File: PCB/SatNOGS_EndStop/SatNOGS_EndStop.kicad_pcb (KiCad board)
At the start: 2 copper layers, 47 x 14 mm, 7 parts, among them P1 CONN_01X03, U1 TCST2103

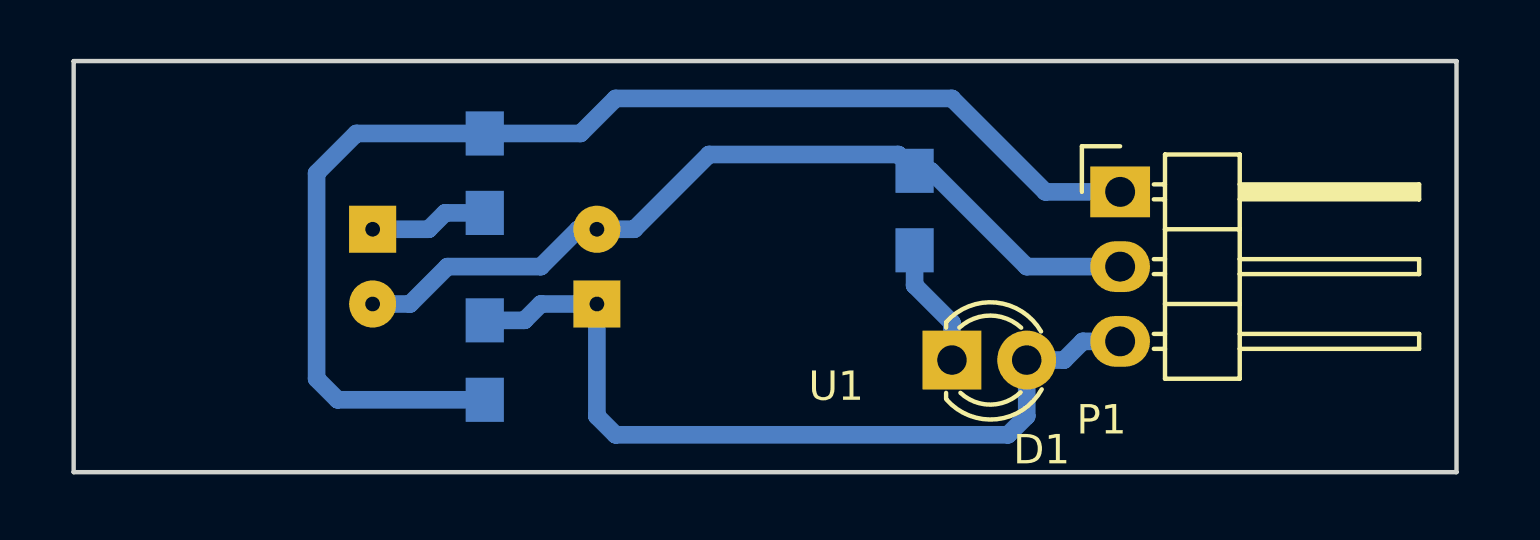
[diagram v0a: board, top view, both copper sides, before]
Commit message: Delete gerber files, update endstop and encoder PCB. Delete gerber files according to repo policy. Update the PCBs with 3d models and small fixes.
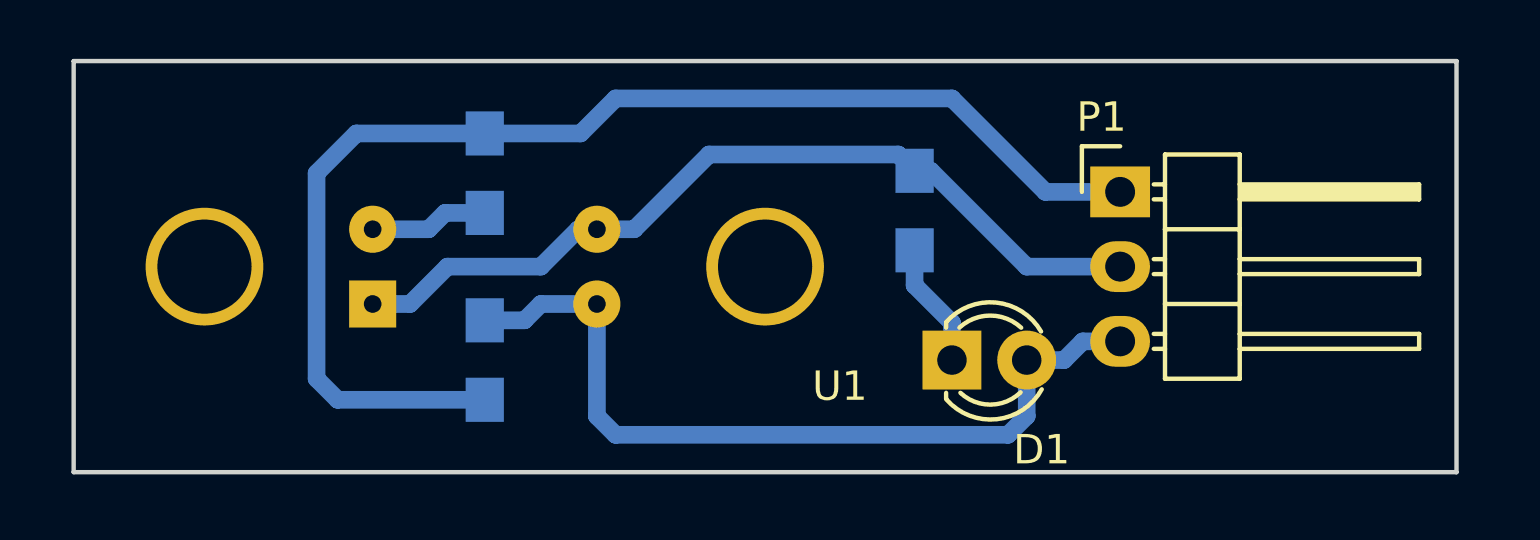
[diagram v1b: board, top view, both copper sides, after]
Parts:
- moved SatNOGS Endstop 37.0 mm to (173.5, 104.5)
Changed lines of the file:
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@@
-(kicad_pcb (version 4) (host pcbnew 0.201509101502+6177~30~ubuntu14.04.1-product)
+(kicad_pcb (version 4) (host pcbnew "(after 2015-mar-04 BZR unknown)-product")
   (general
     (links 10)
     (no_connects 0)
-    (area 132.004999 98.349999 179.145001 112.508)
+    (area 132.004999 98.349999 179.145001 112.470001)
     (thickness 1.6)
     (drawings 4)
@@
     (mod_text_size 1 1)
     (mod_text_width 0.15)
-    (pad_size 1.524 1.524)
-    (pad_drill 0.762)
+    (pad_size 1.6 1.6)
+    (pad_drill 0.6)
     (pad_to_mask_clearance 0.2)
     (aux_axis_origin 0 0)
@@
     (add_net "Net-(R1-Pad2)")
   )
-  (module satnogs:TCST2103 (layer F.Cu)
-    (at 146.05 105.41)
-    (fp_text reference U1 (at 11.938 4.064) (layer F.SilkS)
-      (effects (font (size 1 1) (thickness 0.15)))
-    )
-    (fp_text value TCST2103 (at -8.89 -5.08) (layer F.SilkS) hide
-      (effects (font (size 1 1) (thickness 0.15)))
-    )
-    (fp_circle (center -9.525 0) (end -11.175 0) (layer F.CrtYd) (width 0.15))
-    (fp_circle (center 9.525 0) (end 11.175 0) (layer F.CrtYd) (width 0.15))
-    (fp_line (start -1.5875 -3.1115) (end -1.5875 3.2385) (layer F.CrtYd) (width 0.15))
-    (fp_line (start 1.5875 -3.1115) (end 1.5875 3.175) (layer F.CrtYd) (width 0.15))
-    (fp_line (start -5.969 -3.1115) (end -5.969 3.175) (layer F.CrtYd) (width 0.15))
-    (fp_line (start 5.969 0) (end 5.969 3.175) (layer F.CrtYd) (width 0.15))
-    (fp_line (start 5.969 0) (end 5.969 -3.1115) (layer F.CrtYd) (width 0.15))
-    (fp_line (start -12.7 -3.175) (end -12.7 3.175) (layer F.CrtYd) (width 0.15))
-    (fp_line (start 12.7 -3.175) (end 12.7 3.175) (layer F.CrtYd) (width 0.15))
-    (fp_line (start 12.7 3.175) (end -12.7 3.175) (layer F.CrtYd) (width 0.15))
-    (fp_line (start -12.7 -3.175) (end 12.7 -3.175) (layer F.CrtYd) (width 0.15))
-    (pad 1 thru_hole rect (at -3.81 -1.27) (size 1.6 1.6) (drill 0.5) (layers *.Cu *.Mask F.SilkS)
-      (net 4 "Net-(R1-Pad2)"))
-    (pad 2 thru_hole circle (at -3.81 1.27) (size 1.6 1.6) (drill 0.5) (layers *.Cu *.Mask F.SilkS)
-      (net 2 GND))
-    (pad 3 thru_hole rect (at 3.81 1.27) (size 1.6 1.6) (drill 0.5) (layers *.Cu *.Mask F.SilkS)
-      (net 5 /Signal))
-    (pad 4 thru_hole circle (at 3.81 -1.27) (size 1.6 1.6) (drill 0.5) (layers *.Cu *.Mask F.SilkS)
-      (net 2 GND))
-  )
   (module LEDs:LED-3MM (layer F.Cu)
     (at 161.925 108.585)
@@
       (at (xyz 0.05 0 0))
       (scale (xyz 1 1 1))
-      (rotate (xyz 0 0 90))
+      (rotate (xyz 0 0 0))
     )
   )
@@
     (descr "Through hole pin header")
     (tags "pin header")
-    (fp_text reference P1 (at -0.635 7.747) (layer F.SilkS)
+    (fp_text reference P1 (at -0.635 -2.54) (layer F.SilkS)
       (effects (font (size 1 1) (thickness 0.15)))
     )
@@
   )
   (module Symbols:Symbol_OSHW-Logo_SilkScreen (layer B.Cu)
-    (at 136.525 105.41 180)
+    (at 173.482 104.521 180)
     (descr "Symbol, OSHW-Logo, Silk Screen,")
     (tags "Symbol, OSHW-Logo, Silk Screen,")
-    (fp_text reference "SatNOGS Endstop" (at -0.889 4.953 180) (layer B.SilkS)
+    (fp_text reference "SatNOGS Endstop" (at 1.397 3.937 180) (layer B.SilkS)
       (effects (font (size 0.8 0.8) (thickness 0.15)) (justify mirror))
     )
-    (fp_text value "© Libre Space Foundation" (at -3.81 6.223 180) (layer B.SilkS)
+    (fp_text value "© Libre Space Foundation" (at 4.064 5.207 180) (layer B.SilkS)
       (effects (font (size 0.8 0.8) (thickness 0.15)) (justify mirror))
     )
@@
     (fp_line (start 0.35052 -0.89916) (end 0.7493 -1.89992) (layer B.SilkS) (width 0.15))
   )
+  (module satnogs:TCST2103 (layer F.Cu)
+    (at 146.05 105.41)
+    (fp_text reference U1 (at 12.065 4.064) (layer F.SilkS)
+      (effects (font (size 1 1) (thickness 0.15)))
+    )
+    (fp_text value TCST2103 (at -8.89 -5.08) (layer F.Fab)
+      (effects (font (size 1 1) (thickness 0.15)))
+    )
+    (fp_circle (center -9.525 0) (end -11.175 0) (layer Dwgs.User) (width 0.15))
+    (fp_circle (center 9.525 0) (end 11.175 0) (layer Dwgs.User) (width 0.15))
+    (fp_line (start -1.5875 -3.1115) (end -1.5875 3.2385) (layer F.CrtYd) (width 0.15))
+    (fp_line (start 1.5875 -3.1115) (end 1.5875 3.175) (layer F.CrtYd) (width 0.15))
+    (fp_line (start -5.969 -3.1115) (end -5.969 3.175) (layer F.CrtYd) (width 0.15))
+    (fp_line (start 5.969 0) (end 5.969 3.175) (layer F.CrtYd) (width 0.15))
+    (fp_line (start 5.969 0) (end 5.969 -3.1115) (layer F.CrtYd) (width 0.15))
+    (fp_line (start -12.7 -3.175) (end -12.7 3.175) (layer F.CrtYd) (width 0.15))
+    (fp_line (start 12.7 -3.175) (end 12.7 3.175) (layer F.CrtYd) (width 0.15))
+    (fp_line (start 12.7 3.175) (end -12.7 3.175) (layer F.CrtYd) (width 0.15))
+    (fp_line (start -12.7 -3.175) (end 12.7 -3.175) (layer F.CrtYd) (width 0.15))
+    (pad 1 thru_hole circle (at -3.81 -1.27) (size 1.6 1.6) (drill 0.6) (layers *.Cu *.Mask F.SilkS)
+      (net 4 "Net-(R1-Pad2)"))
+    (pad 2 thru_hole rect (at -3.81 1.27) (size 1.6 1.6) (drill 0.6) (layers *.Cu *.Mask F.SilkS)
+      (net 2 GND))
+    (pad 3 thru_hole circle (at 3.81 1.27) (size 1.6 1.6) (drill 0.6) (layers *.Cu *.Mask F.SilkS)
+      (net 5 /Signal))
+    (pad 4 thru_hole circle (at 3.81 -1.27) (size 1.6 1.6) (drill 0.6) (layers *.Cu *.Mask F.SilkS)
+      (net 2 GND))
+    (pad 5 thru_hole circle (at 9.525 0) (size 4 4) (drill 3.2) (layers *.Cu *.Mask F.SilkS))
+    (pad 6 thru_hole circle (at -9.525 0) (size 4 4) (drill 3.2) (layers *.Cu *.Mask F.SilkS))
+    (model ../../../../../home/azisi/Documents/SatNOGS/satnogs-rotator-controller/PCB/library/satnogs.3dshapes/TCST2103.x3d
+      (at (xyz 0 0 0))
+      (scale (xyz 0.3937 0.3937 0.3937))
+      (rotate (xyz 0 0 0))
+    )
+  )
   (gr_line (start 179.07 98.425) (end 132.08 98.425) (angle 90) (layer Edge.Cuts) (width 0.15))

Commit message: Small fixes.
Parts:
- moved D1 1.14 mm to (160.8, 108.5)
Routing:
- net Net-(D1-Pad1): track 4.89 -> 3.72 mm
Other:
- board text added: "+5V"
- board text added: "GND"
- board text added: "S"
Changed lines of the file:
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@@
   (general
     (links 10)
-    (no_connects 0)
+    (no_connects 3)
     (area 132.004999 98.349999 179.145001 112.470001)
     (thickness 1.6)
-    (drawings 4)
-    (tracks 40)
+    (drawings 7)
+    (tracks 39)
     (zones 0)
     (modules 7)
@@
   )
   (module LEDs:LED-3MM (layer F.Cu)
-    (at 161.925 108.585)
+    (at 160.782 108.5215)
     (descr "LED 3mm round vertical")
     (tags "LED  3mm round vertical")
@@
     )
   )
+  (gr_text S (at 165.4175 107.95) (layer F.SilkS)
+    (effects (font (size 0.8 0.8) (thickness 0.2)))
+  )
+  (gr_text "GND\n" (at 164.592 105.41) (layer F.SilkS)
+    (effects (font (size 0.8 0.8) (thickness 0.2)))
+  )
+  (gr_text +5V (at 164.465 102.87) (layer F.SilkS)
+    (effects (font (size 0.8 0.8) (thickness 0.2)))
+  )
   (gr_line (start 179.07 98.425) (end 132.08 98.425) (angle 90) (layer Edge.Cuts) (width 0.15))
   (gr_line (start 179.07 112.395) (end 179.07 98.425) (angle 90) (layer Edge.Cuts) (width 0.15))
   (gr_line (start 132.08 112.395) (end 179.07 112.395) (angle 90) (layer Edge.Cuts) (width 0.15))
   (gr_line (start 132.08 98.425) (end 132.08 112.395) (angle 90) (layer Edge.Cuts) (width 0.15))
-  (segment (start 160.655 104.855) (end 160.655 106.045) (width 0.6) (layer B.Cu) (net 1))
-  (segment (start 161.925 107.315) (end 161.925 108.585) (width 0.6) (layer B.Cu) (net 1))
-  (segment (start 160.655 106.045) (end 161.925 107.315) (width 0.6) (layer B.Cu) (net 1))
-  (segment (start 161.925 108.585) (end 161.925 107.95) (width 0.6) (layer B.Cu) (net 1))
+  (segment (start 160.655 104.855) (end 160.655 108.3945) (width 0.6) (layer B.Cu) (net 1))
+  (segment (start 160.655 108.3945) (end 160.782 108.5215) (width 0.6) (layer B.Cu) (net 1))
+  (segment (start 149.225 104.14) (end 149.86 104.14) (width 0.6) (layer B.Cu) (net 2))
+  (segment (start 143.51 106.68) (end 144.78 105.41) (width 0.6) (layer B.Cu) (net 2))
+  (segment (start 144.78 105.41) (end 147.955 105.41) (width 0.6) (layer B.Cu) (net 2))
+  (segment (start 147.955 105.41) (end 149.225 104.14) (width 0.6) (layer B.Cu) (net 2))
+  (segment (start 142.24 106.68) (end 143.51 106.68) (width 0.6) (layer B.Cu) (net 2))
+  (segment (start 160.1 101.6) (end 160.655 102.155) (width 0.6) (layer B.Cu) (net 2))
+  (segment (start 151.13 104.14) (end 153.67 101.6) (width 0.6) (layer B.Cu) (net 2))
+  (segment (start 153.67 101.6) (end 160.1 101.6) (width 0.6) (layer B.Cu) (net 2))
+  (segment (start 149.86 104.14) (end 151.13 104.14) (width 0.6) (layer B.Cu) (net 2))
+  (segment (start 164.465 105.41) (end 167.64 105.41) (width 0.6) (layer B.Cu) (net 2))
+  (segment (start 161.21 102.155) (end 164.465 105.41) (width 0.6) (layer B.Cu) (net 2))
   (segment (start 160.655 102.155) (end 161.21 102.155) (width 0.6) (layer B.Cu) (net 2))
-  (segment (start 161.21 102.155) (end 164.465 105.41) (width 0.6) (layer B.Cu) (net 2))
-  (segment (start 164.465 105.41) (end 167.64 105.41) (width 0.6) (layer B.Cu) (net 2))
-  (segment (start 149.86 104.14) (end 151.13 104.14) (width 0.6) (layer B.Cu) (net 2))
-  (segment (start 153.67 101.6) (end 160.1 101.6) (width 0.6) (layer B.Cu) (net 2))
-  (segment (start 151.13 104.14) (end 153.67 101.6) (width 0.6) (layer B.Cu) (net 2))
-  (segment (start 160.1 101.6) (end 160.655 102.155) (width 0.6) (layer B.Cu) (net 2))
-  (segment (start 142.24 106.68) (end 143.51 106.68) (width 0.6) (layer B.Cu) (net 2))
-  (segment (start 147.955 105.41) (end 149.225 104.14) (width 0.6) (layer B.Cu) (net 2))
-  (segment (start 144.78 105.41) (end 147.955 105.41) (width 0.6) (layer B.Cu) (net 2))
-  (segment (start 143.51 106.68) (end 144.78 105.41) (width 0.6) (layer B.Cu) (net 2))
-  (segment (start 149.225 104.14) (end 149.86 104.14) (width 0.6) (layer B.Cu) (net 2))
+  (segment (start 149.305 100.885) (end 150.495 99.695) (width 0.6) (layer B.Cu) (net 3))
+  (segment (start 150.495 99.695) (end 161.925 99.695) (width 0.6) (layer B.Cu) (net 3))
+  (segment (start 161.925 99.695) (end 165.1 102.87) (width 0.6) (layer B.Cu) (net 3))
+  (segment (start 165.1 102.87) (end 167.64 102.87) (width 0.6) (layer B.Cu) (net 3))
+  (segment (start 146.05 100.885) (end 149.305 100.885) (width 0.6) (layer B.Cu) (net 3))
+  (segment (start 141.05 109.935) (end 140.335 109.22) (width 0.6) (layer B.Cu) (net 3))
+  (segment (start 140.335 109.22) (end 140.335 102.235) (width 0.6) (layer B.Cu) (net 3))
+  (segment (start 140.335 102.235) (end 141.685 100.885) (width 0.6) (layer B.Cu) (net 3))
+  (segment (start 141.685 100.885) (end 146.05 100.885) (width 0.6) (layer B.Cu) (net 3))
   (segment (start 146.05 109.935) (end 141.05 109.935) (width 0.6) (layer B.Cu) (net 3))
-  (segment (start 141.685 100.885) (end 146.05 100.885) (width 0.6) (layer B.Cu) (net 3))
-  (segment (start 140.335 102.235) (end 141.685 100.885) (width 0.6) (layer B.Cu) (net 3))
-  (segment (start 140.335 109.22) (end 140.335 102.235) (width 0.6) (layer B.Cu) (net 3))
-  (segment (start 141.05 109.935) (end 140.335 109.22) (width 0.6) (layer B.Cu) (net 3))
-  (segment (start 146.05 100.885) (end 149.305 100.885) (width 0.6) (layer B.Cu) (net 3))
-  (segment (start 165.1 102.87) (end 167.64 102.87) (width 0.6) (layer B.Cu) (net 3))
-  (segment (start 161.925 99.695) (end 165.1 102.87) (width 0.6) (layer B.Cu) (net 3))
-  (segment (start 150.495 99.695) (end 161.925 99.695) (width 0.6) (layer B.Cu) (net 3))
-  (segment (start 149.305 100.885) (end 150.495 99.695) (width 0.6) (layer B.Cu) (net 3))
+  (segment (start 144.145 104.14) (end 144.7 103.585) (width 0.6) (layer B.Cu) (net 4))
+  (segment (start 144.7 103.585) (end 146.05 103.585) (width 0.6) (layer B.Cu) (net 4))
   (segment (start 142.24 104.14) (end 144.145 104.14) (width 0.6) (layer B.Cu) (net 4))
-  (segment (start 144.7 103.585) (end 146.05 103.585) (width 0.6) (layer B.Cu) (net 4))
-  (segment (start 144.145 104.14) (end 144.7 103.585) (width 0.6) (layer B.Cu) (net 4))
-  (segment (start 164.465 108.585) (end 165.735 108.585) (width 0.6) (layer B.Cu) (net 5))
-  (segment (start 166.37 107.95) (end 167.64 107.95) (width 0.6) (layer B.Cu) (net 5))
-  (segment (start 165.735 108.585) (end 166.37 107.95) (width 0.6) (layer B.Cu) (net 5))
+  (segment (start 163.322 108.5215) (end 163.3347 108.5342) (width 0.6) (layer B.Cu) (net 5))
+  (segment (start 163.3347 108.5342) (end 165.6588 108.5342) (width 0.6) (layer B.Cu) (net 5))
+  (segment (start 165.6588 108.5342) (end 166.243 107.95) (width 0.6) (layer B.Cu) (net 5))
+  (segment (start 166.243 107.95) (end 167.64 107.95) (width 0.6) (layer B.Cu) (net 5))
+  (segment (start 149.86 106.68) (end 149.86 110.49) (width 0.6) (layer B.Cu) (net 5))
+  (segment (start 149.86 110.49) (end 150.495 111.125) (width 0.6) (layer B.Cu) (net 5))
+  (segment (start 163.322 110.49) (end 163.322 108.5215) (width 0.6) (layer B.Cu) (net 5))
+  (segment (start 150.495 111.125) (end 162.687 111.125) (width 0.6) (layer B.Cu) (net 5))
+  (segment (start 162.687 111.125) (end 163.322 110.49) (width 0.6) (layer B.Cu) (net 5))
+  (segment (start 147.955 106.68) (end 147.4 107.235) (width 0.6) (layer B.Cu) (net 5))
+  (segment (start 147.4 107.235) (end 146.05 107.235) (width 0.6) (layer B.Cu) (net 5))
   (segment (start 149.86 106.68) (end 147.955 106.68) (width 0.6) (layer B.Cu) (net 5))
-  (segment (start 147.4 107.235) (end 146.05 107.235) (width 0.6) (layer B.Cu) (net 5))
-  (segment (start 147.955 106.68) (end 147.4 107.235) (width 0.6) (layer B.Cu) (net 5))
-  (segment (start 164.465 108.585) (end 164.465 110.49) (width 0.6) (layer B.Cu) (net 5))
-  (segment (start 149.86 110.49) (end 149.86 106.68) (width 0.6) (layer B.Cu) (net 5))
-  (segment (start 150.495 111.125) (end 149.86 110.49) (width 0.6) (layer B.Cu) (net 5))
-  (segment (start 163.83 111.125) (end 150.495 111.125) (width 0.6) (layer B.Cu) (net 5))
-  (segment (start 164.465 110.49) (end 163.83 111.125) (width 0.6) (layer B.Cu) (net 5))
   (zone (net 2) (net_name GND) (layer B.Cu) (hatch edge 0.508)
     (connect_pads (clearance 0.8))

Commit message: Update 3d model of PCB and BOM.
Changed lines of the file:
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@@
-(kicad_pcb (version 4) (host pcbnew "(after 2015-mar-04 BZR unknown)-product")
+(kicad_pcb (version 4) (host pcbnew 4.0.1-stable)
   (general
     (links 10)
-    (no_connects 3)
+    (no_connects 0)
     (area 132.004999 98.349999 179.145001 112.470001)
     (thickness 1.6)
@@
       (at (xyz 0.05 0 0))
       (scale (xyz 1 1 1))
-      (rotate (xyz 0 0 0))
+      (rotate (xyz 0 0 90))
     )
   )
@@
     (descr "Through hole pin header")
     (tags "pin header")
-    (fp_text reference P1 (at -0.635 -2.54) (layer F.SilkS)
+    (fp_text reference P1 (at -0.635 -2.54) (layer F.SilkS) hide
       (effects (font (size 1 1) (thickness 0.15)))
     )
@@
   (module satnogs:TCST2103 (layer F.Cu)
     (at 146.05 105.41)
-    (fp_text reference U1 (at 12.065 4.064) (layer F.SilkS)
-      (effects (font (size 1 1) (thickness 0.15)))
-    )
-    (fp_text value TCST2103 (at -8.89 -5.08) (layer F.Fab)
+    (fp_text reference U1 (at 11.43 5.08) (layer F.SilkS)
+      (effects (font (size 1 1) (thickness 0.15)))
+    )
+    (fp_text value TCST2103 (at -8.89 -5.08) (layer F.Fab) hide
       (effects (font (size 1 1) (thickness 0.15)))
     )
@@
     (pad 5 thru_hole circle (at 9.525 0) (size 4 4) (drill 3.2) (layers *.Cu *.Mask F.SilkS))
     (pad 6 thru_hole circle (at -9.525 0) (size 4 4) (drill 3.2) (layers *.Cu *.Mask F.SilkS))
-    (model ../../../../../home/azisi/Documents/SatNOGS/satnogs-rotator-controller/PCB/library/satnogs.3dshapes/TCST2103.x3d
+    (model ../../../../../home/azisi/Documents/SatNOGS/satnogs-rotator-controller/PCB/library/satnogs.3dshapes/TCST2103.wrl
       (at (xyz 0 0 0))
       (scale (xyz 0.3937 0.3937 0.3937))
